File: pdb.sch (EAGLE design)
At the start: 50 parts, among them J1 XT60PWFEMALE, Q1 IRFR5305PBF, Q2 IRFR5305PBF, Q3 BSN20,215, Q4 BSN20,215, Q5 BSN20,215, U1 TSR_1-2433, U2 TXB0104, U3 ATMEGA48-20AU, U4 LTC2946CMSPBF, U5 LTC2946CMSPBF, U6 LTC2946CMSPBF, U7 AT30TS74SS8M

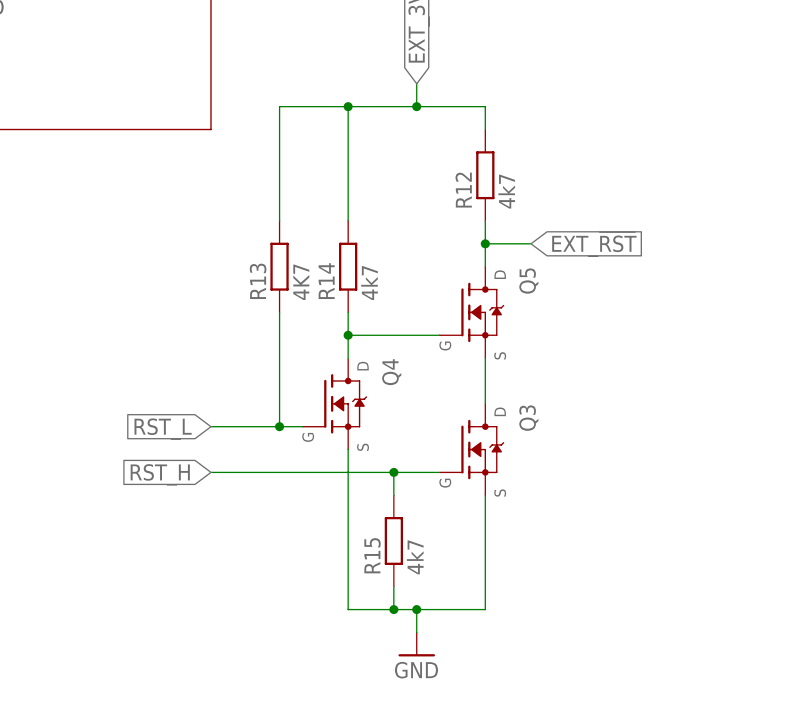
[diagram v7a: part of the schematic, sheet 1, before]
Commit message: fixed layout, silkscreen, resistor values
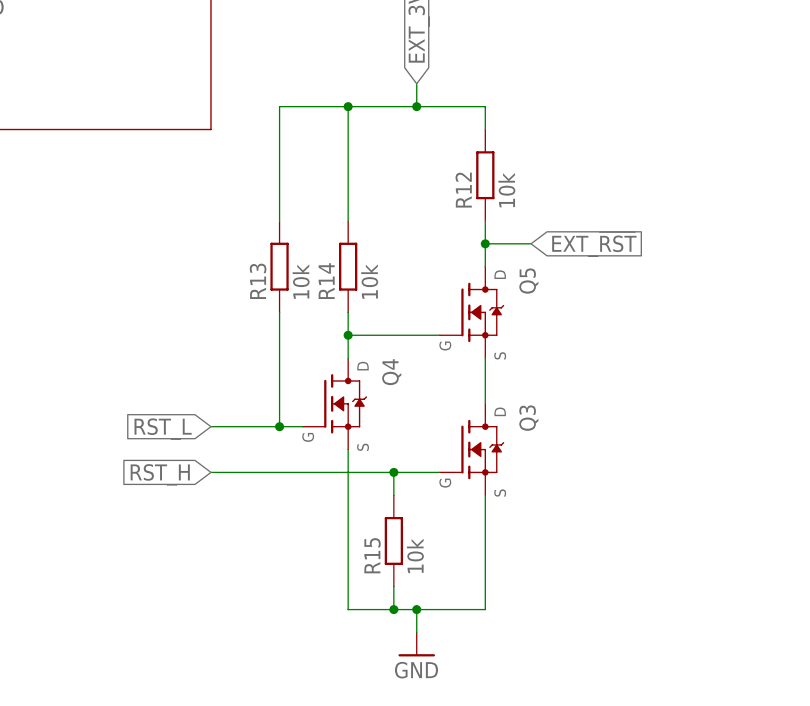
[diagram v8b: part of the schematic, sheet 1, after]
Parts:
- R12, R14, R15: value 4k7 -> 10k
- R13: value 4K7 -> 10k
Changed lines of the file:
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@@
 <part name="SUPPLY19" library="supply2" library_urn="urn:adsk.eagle:library:372" deviceset="+5V" device=""/>
 <part name="+3V1" library="supply1" deviceset="+3V3" device=""/>
-<part name="R14" library="rcl" library_urn="urn:adsk.eagle:library:334" deviceset="R-EU_" device="R0603" package3d_urn="urn:adsk.eagle:package:23555/2" value="4k7"/>
-<part name="R12" library="rcl" library_urn="urn:adsk.eagle:library:334" deviceset="R-EU_" device="R0603" package3d_urn="urn:adsk.eagle:package:23555/2" value="4k7"/>
-<part name="R13" library="rcl" library_urn="urn:adsk.eagle:library:334" deviceset="R-EU_" device="R0603" package3d_urn="urn:adsk.eagle:package:23555/2" value="4K7"/>
-<part name="R15" library="rcl" library_urn="urn:adsk.eagle:library:334" deviceset="R-EU_" device="R0603" package3d_urn="urn:adsk.eagle:package:23555/2" value="4k7"/>
-<part name="Q4" library="jonas_mosfet" library_urn="urn:adsk.eagle:library:2195717" deviceset="BSN20,215" device="" package3d_urn="urn:adsk.eagle:package:2195720/3"/>
-<part name="Q5" library="jonas_mosfet" library_urn="urn:adsk.eagle:library:2195717" deviceset="BSN20,215" device="" package3d_urn="urn:adsk.eagle:package:2195720/3"/>
-<part name="Q3" library="jonas_mosfet" library_urn="urn:adsk.eagle:library:2195717" deviceset="BSN20,215" device="" package3d_urn="urn:adsk.eagle:package:2195720/3"/>
+<part name="R14" library="rcl" library_urn="urn:adsk.eagle:library:334" deviceset="R-EU_" device="R0603" package3d_urn="urn:adsk.eagle:package:23555/2" value="10k"/>
+<part name="R12" library="rcl" library_urn="urn:adsk.eagle:library:334" deviceset="R-EU_" device="R0603" package3d_urn="urn:adsk.eagle:package:23555/2" value="10k"/>
+<part name="R13" library="rcl" library_urn="urn:adsk.eagle:library:334" deviceset="R-EU_" device="R0603" package3d_urn="urn:adsk.eagle:package:23555/2" value="10k"/>
+<part name="R15" library="rcl" library_urn="urn:adsk.eagle:library:334" deviceset="R-EU_" device="R0603" package3d_urn="urn:adsk.eagle:package:23555/2" value="10k"/>
+<part name="Q4" library="jonas_mosfet" library_urn="urn:adsk.eagle:library:2195717" deviceset="BSN20,215" device="" package3d_urn="urn:adsk.eagle:package:2195720/4"/>
+<part name="Q5" library="jonas_mosfet" library_urn="urn:adsk.eagle:library:2195717" deviceset="BSN20,215" device="" package3d_urn="urn:adsk.eagle:package:2195720/4"/>
+<part name="Q3" library="jonas_mosfet" library_urn="urn:adsk.eagle:library:2195717" deviceset="BSN20,215" device="" package3d_urn="urn:adsk.eagle:package:2195720/4"/>
 <part name="GND21" library="supply1" deviceset="GND" device=""/>
 </parts>
